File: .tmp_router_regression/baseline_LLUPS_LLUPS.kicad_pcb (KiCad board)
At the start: 2 copper layers, 140 x 90 mm, 39 parts, among them J1 USB_C, J2 Output, J3 Debug, Q1 FS8205A, U1 USBLC6-2SC6, U2 BQ24072, U3 HY2113-KB5B, U4 MT3608, U5 AP2112K-3.3, U6 LN61CN3302MR-G

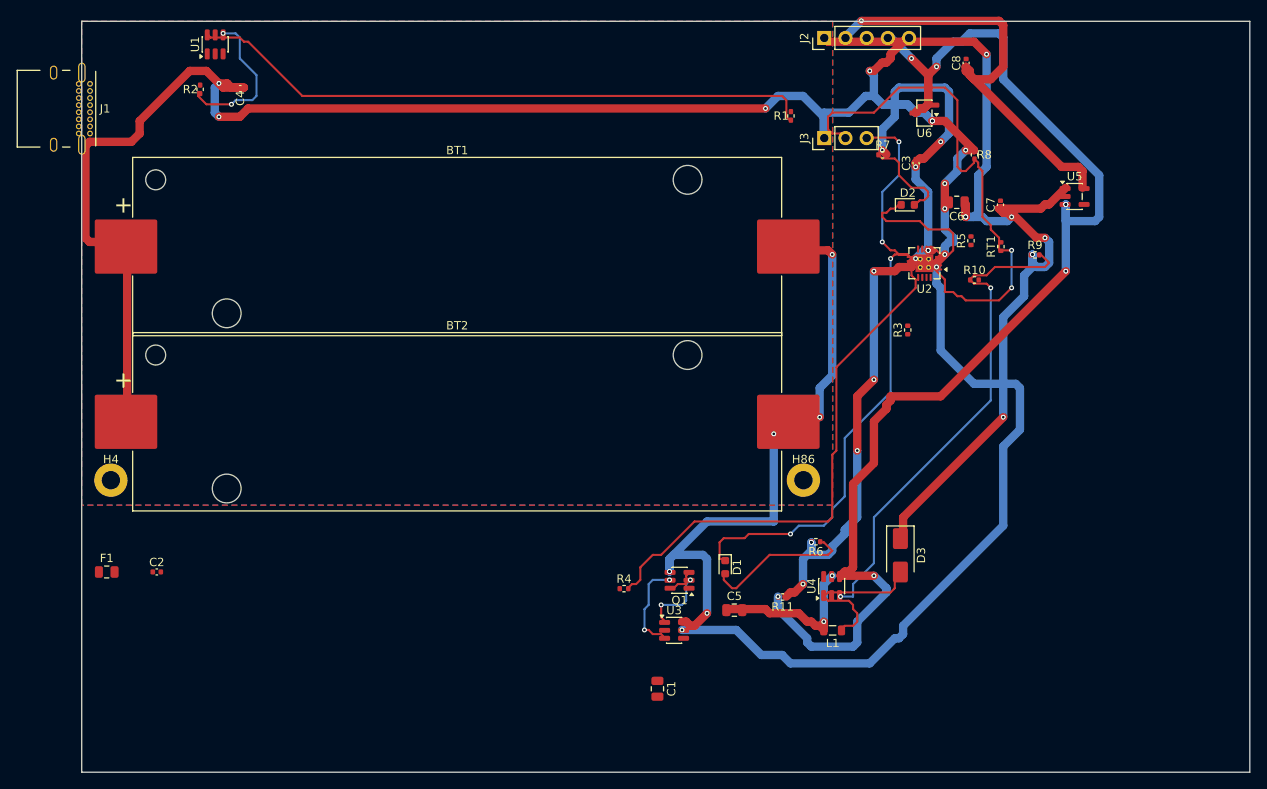
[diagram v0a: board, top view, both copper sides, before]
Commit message: 35-round experiment: best score 25.33, improved routing params
Router and conflict resolution tuning from autonomous optimization loop.
Best config: clearance=0.2051mm, cooling_factor=0.9735, existing_trace_cost=200.0

Co-Authored-By: Claude Opus 4.6 <noreply@anthropic.com>
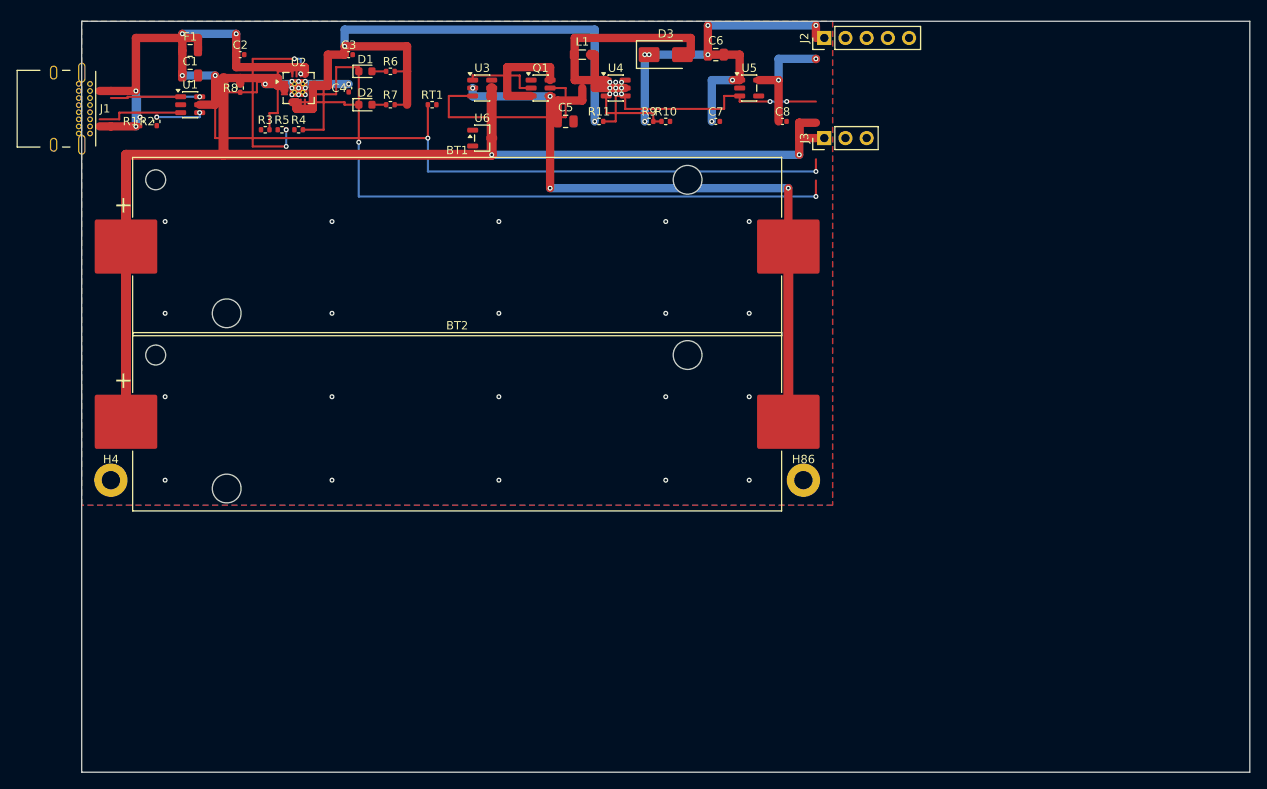
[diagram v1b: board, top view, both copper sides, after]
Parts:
- moved C1 92.4 mm to (13.0, 6.50), turned to 0 degrees
- moved R8 88.4 mm to (19.0, 8.00), turned to 90 degrees
- moved R5 83.6 mm to (24.0, 13.0), turned to 0 degrees
- moved R3 80.7 mm to (22.0, 13.0), turned to 0 degrees
- moved R1 78.0 mm to (7.00, 12.0)
- moved U2 77.9 mm to (26.0, 8.00), turned to 0 degrees
- moved R6 76.0 mm to (37.0, 6.00), turned to 0 degrees
- moved L1 75.2 mm to (60.0, 4.00), turned to 0 degrees
- moved D1 73.4 mm to (34.0, 6.00), turned to 0 degrees
- moved RT1 70.3 mm to (42.0, 10.0), turned to 0 degrees
- moved C3 69.2 mm to (32.0, 4.00), turned to 0 degrees
- moved U3 68.9 mm to (48.0, 8.00)
- moved R4 67.4 mm to (26.0, 13.0)
- moved D3 66.3 mm to (70.0, 4.00), turned to 0 degrees
- moved D2 66.1 mm to (34.0, 10.0)
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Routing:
- net /VBAT: track 293.0 -> 160.5 mm, vias 14 -> 4
- net /EN: track 149.0 -> 32.3 mm, vias 8 -> 2
- net /5V: track 115.5 -> 48.7 mm
- net Net-(R1-Pad1): track 75.5 -> 9.58 mm, vias 0 -> 2
- net Net-(U2-ILIM): track 62.7 -> 9.54 mm
- net Net-(U4-FB): track 60.0 -> 9.68 mm, vias 2 -> 0
- net /3V3: track 52.5 -> 14.4 mm
- net /VBUS: track 0.00 -> 33.8 mm, vias 0 -> 4
- net /NTC_SENSE: track 62.8 -> 96.5 mm
- net Net-(F1-Pad2): track 0.00 -> 28.2 mm, vias 0 -> 2
- net Net-(U2-TMR): track 0.00 -> 24.1 mm, vias 0 -> 4
- net /VSYS: track 93.0 -> 75.0 mm, vias 12 -> 2
- net Net-(D1-A): track 17.7 -> 1.70 mm
- net Net-(Q1B-G): track 11.3 -> 24.8 mm, vias 2 -> 0
- net Net-(R2-Pad1): track 18.4 -> 5.68 mm
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
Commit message: 45-round experiment: best score 25.66, all nets routed (26/26)
Fixed A* performance by increasing max_search from 100k->500k to handle
high trace costs (100.0) without timing out. Kept high cost + coarse grid
(0.5mm) to prevent shorts while still routing efficiently.

Best config: edge_margin=5.7493mm, cooling_factor=0.9764, existing_trace_cost=200, max_rips=8

Co-Authored-By: Claude Opus 4.6 <noreply@anthropic.com>
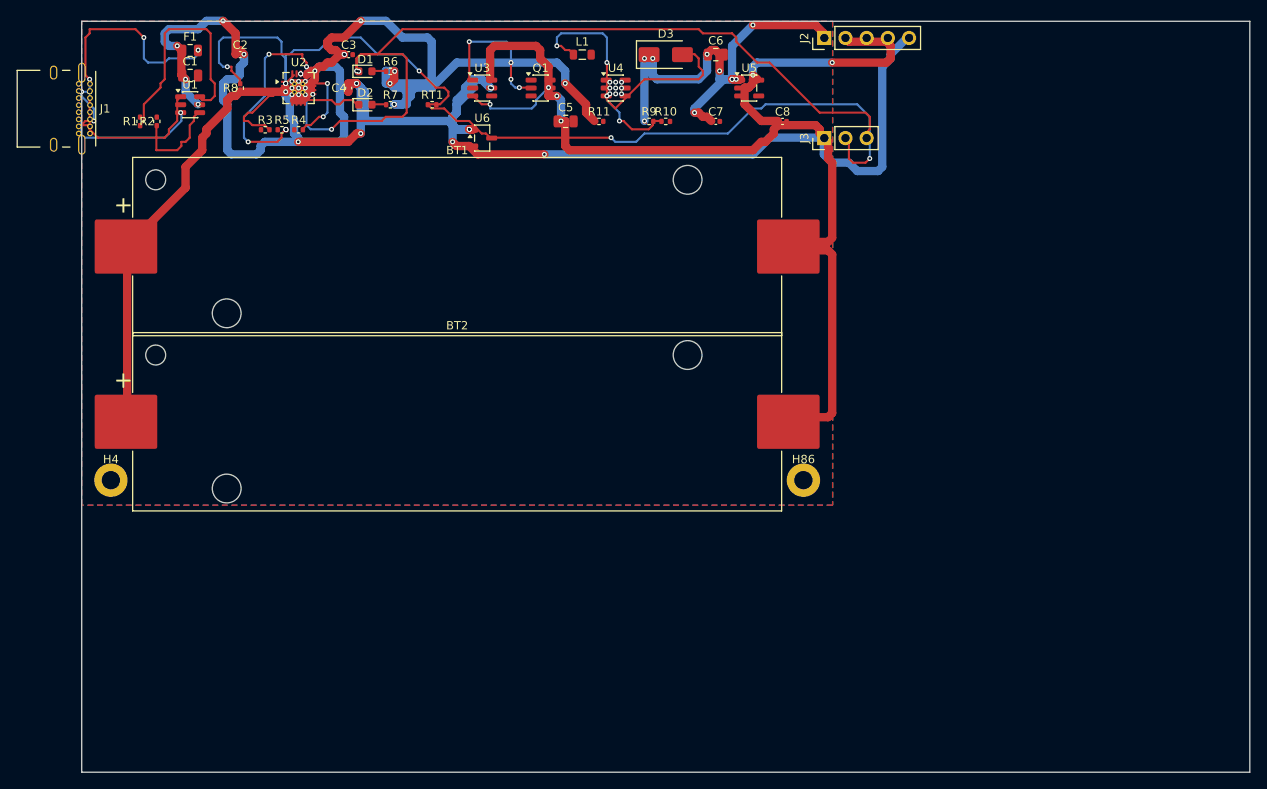
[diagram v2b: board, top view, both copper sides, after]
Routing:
- net /EN: track 32.3 -> 0.00 mm, vias 2 -> 0
- net /VBUS: track 33.8 -> 65.9 mm, vias 4 -> 6
- net /VBAT: track 160.5 -> 189.5 mm, vias 4 -> 14
- net /CELL_NEG: track 77.9 -> 106.3 mm, vias 4 -> 2
- net /CHG_N: track 81.0 -> 104.0 mm, vias 2 -> 4
- net /NTC_SENSE: track 96.5 -> 117.6 mm, vias 2 -> 6
- net /3V3: track 14.4 -> 35.1 mm
- net Net-(R1-Pad1): track 9.58 -> 28.3 mm, vias 2 -> 0
- net /VSYS_BOOST: track 15.2 -> 0.00 mm, vias 0 -> 1
- net Net-(Q1B-G): track 24.8 -> 11.2 mm, vias 0 -> 2
- net Net-(Q1A-D): track 13.0 -> 0.00 mm
- net Net-(J1-CC1): track 8.51 -> 19.2 mm
- net Net-(D3-A): track 25.7 -> 35.3 mm, vias 0 -> 2
- net Net-(Q1A-G): track 9.05 -> 17.4 mm, vias 0 -> 4
- net /5V: track 48.7 -> 55.0 mm, vias 8 -> 10
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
